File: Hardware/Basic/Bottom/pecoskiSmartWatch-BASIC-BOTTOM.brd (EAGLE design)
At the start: 33 x 33 mm, 31 parts, among them U1 AD5242-SO16

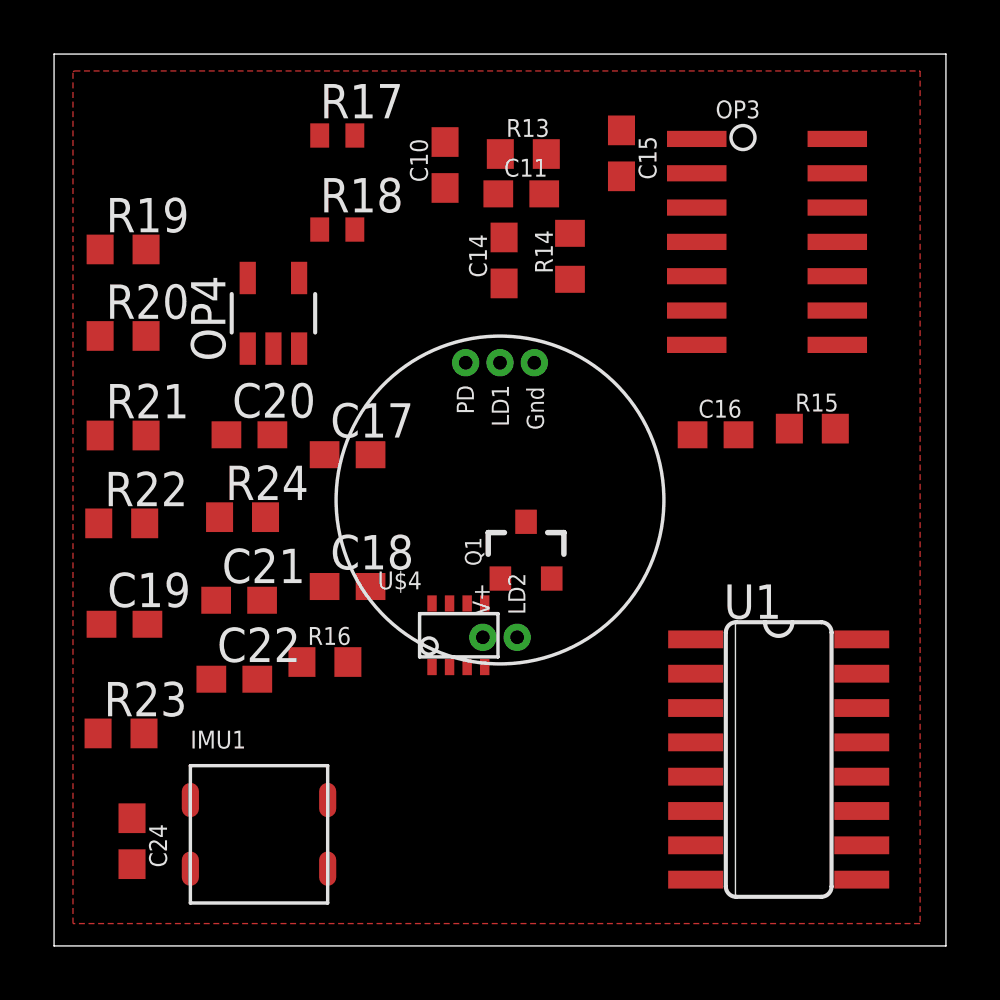
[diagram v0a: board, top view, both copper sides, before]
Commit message: Updated Eagle Hardware 2021_02_27
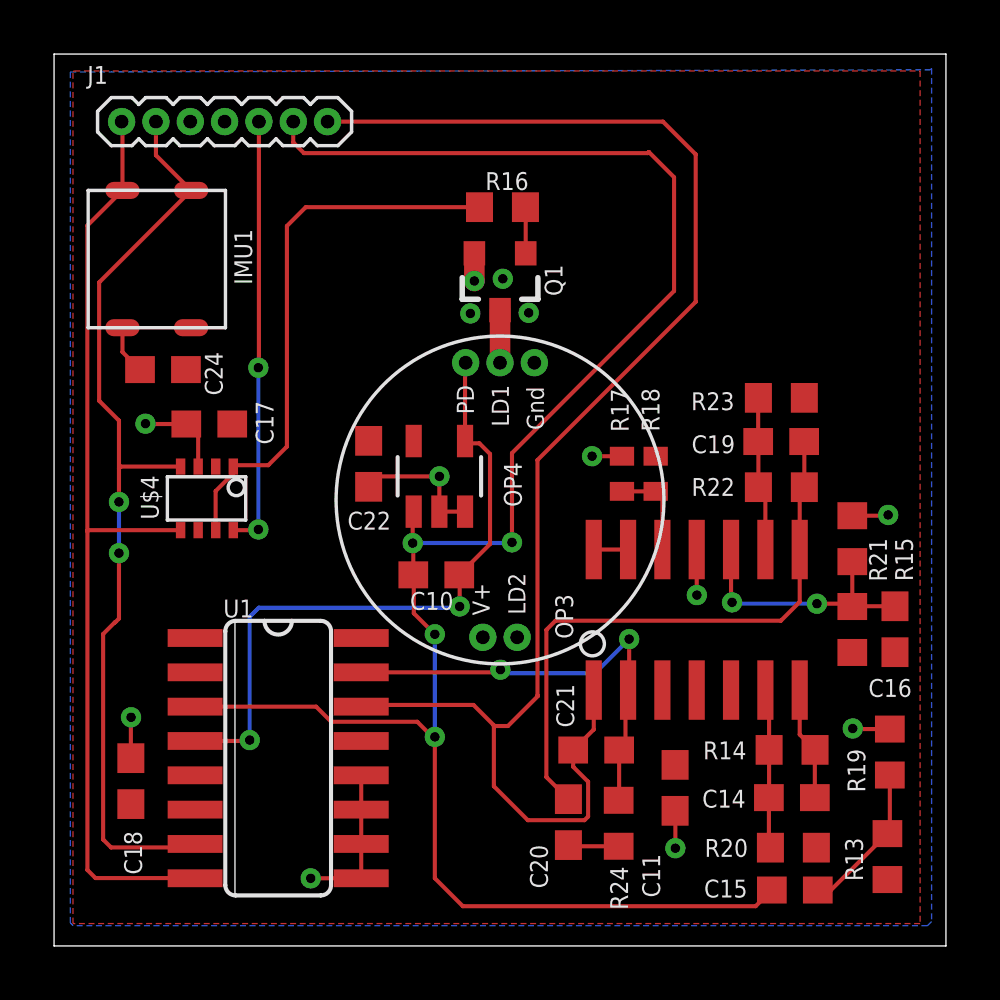
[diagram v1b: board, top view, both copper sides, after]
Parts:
- added J1: (no value), LinnesLab-Connectors:1X07_1.27MM
- moved R19 33.9 mm to (33.4, 9.67), turned to 270 degrees
- moved R20 31.2 mm to (29.9, 6.14), turned to 180 degrees
- moved R13 29.3 mm to (33.3, 5.81), turned to 270 degrees
- moved C15 28.0 mm to (29.9, 4.57), turned to 0 degrees
- moved R23 27.4 mm to (29.4, 22.8), turned to 180 degrees
- moved R21 27.2 mm to (32.0, 17.6), turned to 270 degrees
- moved C19 25.2 mm to (29.4, 21.2), turned to 180 degrees
- moved R22 24.4 mm to (29.4, 19.5)
- moved C11 22.7 mm to (25.5, 8.35), turned to 90 degrees
- moved C14 22.5 mm to (29.8, 7.99), turned to 180 degrees
- moved IMU1 21.6 mm to (6.30, 27.9), turned to 90 degrees
- moved R14 20.0 mm to (29.8, 9.75), turned to 0 degrees
- moved C20 18.6 mm to (21.5, 7.08), turned to 270 degrees
- moved U1 18.5 mm to (10.8, 9.45)
- moved R16 18.1 mm to (19.1, 29.8)
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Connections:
- removed net LED: Q1.3
- removed net LED.CTRL: U$4.8
- removed net PPG: C21.2, OP3.1, U1.14
- removed net TIA: C10.2, C15.1, OP4.1, U1.3
- new net A6/TIA: C10.2, C15.1, J1.6, OP4.1, U1.3
- new net A7/PPG: C21.2, J1.7, OP3.1, U1.14
- new net D29/LED.CTRL: J1.5, U$4.8
- net 3.3V: now also J1.4
- net GND: now also J1.3
- net LED.C: now also Q1.3
- net SCL: now also J1.2
- net SDA: now also J1.1
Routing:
- net A6/TIA: track 0.00 -> 71.5 mm, vias 0 -> 4
- net A7/PPG: track 0.00 -> 55.5 mm
- net SDA: track 0.00 -> 35.8 mm
- net SCL: track 0.00 -> 35.0 mm, vias 0 -> 2
- net GND: track 0.00 -> 25.2 mm, vias 0 -> 13
- net PD.C: track 0.00 -> 24.7 mm, vias 0 -> 2
- net N$19: track 0.00 -> 22.5 mm
- net N$9: track 0.00 -> 20.5 mm
- net G.W2: track 0.00 -> 16.7 mm, vias 0 -> 2
- net D29/LED.CTRL: track 0.00 -> 16.0 mm, vias 0 -> 2
- net N$17: track 0.00 -> 9.73 mm, vias 0 -> 2
- net N$15: track 0.00 -> 5.91 mm
- net N$18: track 0.00 -> 5.73 mm
- net N$13: track 0.00 -> 5.65 mm
- net N$16: track 0.00 -> 4.22 mm
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- added copper zone on layer 16, net GND

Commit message: Hardware Updates 2021_02_27
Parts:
- moved R23 0.53 mm to (29.4, 23.3)
- moved R20 0.48 mm to (29.7, 6.59)
- moved R15 0.45 mm to (31.7, 14.5)
- moved R14 0.42 mm to (29.7, 10.2)
- moved C16 0.38 mm to (33.4, 14.6)
- moved C14 0.36 mm to (29.7, 8.32)
- moved R21 0.34 mm to (32.0, 17.9)
- moved OP3 0.34 mm to (26.2, 14.9)
- moved R13 0.33 mm to (33.4, 5.48)
- moved C19 0.28 mm to (29.4, 21.4)
- moved R22 0.28 mm to (29.4, 19.8)
- moved R17 0.26 mm to (24.7, 20.2)
- moved R18 0.26 mm to (23.5, 20.2)
- moved C21 0.19 mm to (22.6, 9.94)
- renumbered OP4 to TIA, U$4 to AD517, U1 to AD5242
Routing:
- net VREF: track 1.27 -> 34.1 mm, vias 0 -> 3
- net N$13: track 5.65 -> 16.1 mm
- net N$16: track 4.22 -> 8.72 mm
- net GND: track 25.2 -> 26.6 mm, vias 13 -> 14
- net N$17: track 9.73 -> 10.9 mm

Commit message: HW Updates 2021/03/06
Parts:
- added C1: 100n, LinnesLab-Passives:C0603
- added LOGO1: REVISION.A, LinnesLab-Logos:REV.A
- added LOGO2: OSHW-LOGOS, LinnesLab-Logos:OSHW-LOGO-S
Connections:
- net GND: now also C1.2
- net VREF: now also C1.1
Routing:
- net GND: track 26.6 -> 28.2 mm, vias 14 -> 15
- net VREF: track 34.1 -> 35.5 mm
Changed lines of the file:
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@@
 <attribute name="VALUE" x="3.73" y="30.968" locked="yes" size="0.6096" layer="27" font="vector" ratio="20"/>
 </element>
+<element name="C1" library="LinnesLab-Passives" package="C0603" value="100n" x="28.582625" y="26.461721875" smashed="yes" rot="R90">
+<attribute name="NAME" x="27.614884375" y="26.174703125" size="0.7112" layer="25" rot="R90"/>
+<attribute name="VALUE" x="30.487625" y="25.826721875" size="1.27" layer="27" rot="R90"/>
+</element>
+<element name="LOGO1" library="LinnesLab-Logos" package="REV.A" value="REVISION.A" x="4.03098125" y="3.850640625" smashed="yes"/>
+<element name="LOGO2" library="LinnesLab-Logos" package="OSHW-LOGO-S" value="OSHW-LOGOS" x="32.19958125" y="32.362140625" smashed="yes"/>
 </elements>
 <signals>
@@
 <wire x1="5.0317375" y1="26.037534375" x2="5.509259375" y2="26.51505625" width="0.1524" layer="1"/>
 <via x="5.509259375" y="26.51505625" extent="1-16" drill="0.35"/>
+<contactref element="C1" pad="2"/>
+<wire x1="28.582625" y1="27.311721875" x2="28.582625" y2="28.897584375" width="0.1524" layer="1"/>
+<wire x1="28.582625" y1="28.897584375" x2="28.5877" y2="28.902659375" width="0.1524" layer="1"/>
+<via x="28.5877" y="28.902659375" extent="1-16" drill="0.35"/>
 </signal>
 <signal name="3.3V">
@@
 <wire x1="22.438353125" y1="19.959690625" x2="21.7731375" y2="20.62490625" width="0.1524" layer="1"/>
 <wire x1="21.7731375" y1="20.62490625" x2="21.7731375" y2="21.19655625" width="0.1524" layer="1"/>
-<wire x1="21.7731375" y1="21.19655625" x2="25.1968" y2="24.62021875" width="0.1524" layer="1"/>
-<wire x1="30.2759" y1="24.252821875" x2="30.2759" y2="23.340059375" width="0.1524" layer="1"/>
-<wire x1="30.2759" y1="23.340059375" x2="30.242878125" y2="23.3070375" width="0.1524" layer="1"/>
-<wire x1="25.1968" y1="24.62021875" x2="29.908503125" y2="24.62021875" width="0.1524" layer="1"/>
-<wire x1="29.908503125" y1="24.62021875" x2="30.2759" y2="24.252821875" width="0.1524" layer="1"/>
+<wire x1="30.242878125" y1="23.309578125" x2="30.242878125" y2="23.3070375" width="0.1524" layer="1"/>
 <wire x1="30.562915625" y1="6.591296875" x2="31.292796875" y2="6.591296875" width="0.1524" layer="1"/>
 <wire x1="31.292796875" y1="6.591296875" x2="31.709359375" y2="7.007859375" width="0.1524" layer="1"/>
@@
 <wire x1="23.6728" y1="15.621" x2="25.003759375" y2="14.290040625" width="0.1524" layer="16"/>
 <wire x1="25.003759375" y1="14.290040625" x2="25.003759375" y2="14.26998125" width="0.1524" layer="16"/>
+<contactref element="C1" pad="1"/>
+<wire x1="26.188303125" y1="25.611721875" x2="28.582625" y2="25.611721875" width="0.1524" layer="1"/>
+<wire x1="21.7731375" y1="21.19655625" x2="26.188303125" y2="25.611721875" width="0.1524" layer="1"/>
+<wire x1="28.582625" y1="25.611721875" x2="29.793296875" y2="25.611721875" width="0.1524" layer="1"/>
+<wire x1="29.793296875" y1="25.611721875" x2="30.261559375" y2="25.143459375" width="0.1524" layer="1"/>
+<wire x1="30.261559375" y1="25.143459375" x2="30.261559375" y2="23.328259375" width="0.1524" layer="1"/>
+<wire x1="30.261559375" y1="23.328259375" x2="30.242878125" y2="23.309578125" width="0.1524" layer="1"/>
 </signal>
 <signal name="N$9">

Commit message: Updated HW 2021_03_13 AM
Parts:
- added C2: 1u, LinnesLab-Passives:C0603
- added U2: PCF8523, LinnesLab-Clocks:SO8
- added Y2: 32.7680kHz, LinnesLab-Clocks:2-SMD.NOLEAD.2.0MMTO1.2MM
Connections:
- new net N$1: U2.2, Y2.P$1
- new net N$2: U2.1, Y2.P$2
- new net VBAT: U2.3
- net 3.3V: now also C2.1, U2.8
- net GND: now also C2.2, U2.4
- net SCL: now also U2.6
- net SDA: now also U2.5

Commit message: Updated HW 2021_03_13 PM
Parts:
- added C3, C4: 4.7u, LinnesLab-Passives:C0603
- added C6, C9: 1u, LinnesLab-Passives:C0603
- added CHRG: MCP73831, LinnesLab-Power:SOT23-5
- added LDO1: MIC5504, LinnesLab-Power:SOT23-5
- added R3: 100k, LinnesLab-Passives:R0603
- added R4: (no value), LinnesLab-Passives:R0603
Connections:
- new net D27/CHRG.STATUS: CHRG.1, R3.1
- new net N$3: CHRG.5, R4.2
- new net VIN1: C4.2, C6.2, CHRG.4, LDO1.1, LDO1.3, R3.2
- new net VLIPO: C3.1, CHRG.3
- net 3.3V: now also C9.1, LDO1.5
- net GND: now also C3.2, C4.1, C6.1, C9.2, CHRG.2, LDO1.2, R4.1
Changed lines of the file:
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@@
 <attribute name="VALUE" x="-13.675359375" y="-7.566659375" size="0.7112" layer="27"/>
+</element>
+<element name="CHRG" library="LinnesLab-Power" package="SOT23-5" value="MCP73831" x="-12.36218125" y="-14.54658125" smashed="yes">
+<attribute name="NAME" x="-14.26718125" y="-14.54658125" size="0.6096" layer="25" ratio="20" rot="R90" align="bottom-center"/>
+<attribute name="PROD_ID" value="IC-09995" x="-12.36218125" y="-14.157959375" size="1.778" layer="27" display="off"/>
+<attribute name="VALUE" x="-9.82218125" y="-14.54658125" size="0.6096" layer="27" ratio="20" rot="R90" align="bottom-center"/>
+</element>
+<element name="LDO1" library="LinnesLab-Power" package="SOT23-5" value="MIC5504" x="-9.357359375" y="-23.014940625" smashed="yes">
+<attribute name="NAME" x="-11.262359375" y="-23.014940625" size="0.6096" layer="25" ratio="20" rot="R90" align="bottom-center"/>
+<attribute name="VALUE" x="-6.817359375" y="-23.014940625" size="0.6096" layer="27" ratio="20" rot="R90" align="bottom-center"/>
+</element>
+<element name="C6" library="LinnesLab-Passives" package="C0603" package3d_urn="urn:adsk.eagle:package:15661989/2" value="1u" x="-7.49808125" y="-18.59788125" smashed="yes">
+<attribute name="NAME" x="-8.13308125" y="-17.96288125" size="0.7112" layer="25"/>
+<attribute name="VALUE" x="-8.13308125" y="-20.50288125" size="0.7112" layer="27"/>
+</element>
+<element name="C9" library="LinnesLab-Passives" package="C0603" package3d_urn="urn:adsk.eagle:package:15661989/2" value="1u" x="-13.67028125" y="-22.672040625" smashed="yes">
+<attribute name="NAME" x="-14.30528125" y="-22.037040625" size="0.7112" layer="25"/>
+<attribute name="VALUE" x="-14.30528125" y="-24.577040625" size="0.7112" layer="27"/>
+</element>
+<element name="C3" library="LinnesLab-Passives" package="C0603" package3d_urn="urn:adsk.eagle:package:15661989/2" value="4.7u" x="-13.67028125" y="-18.59788125" smashed="yes">
+<attribute name="NAME" x="-14.30528125" y="-17.96288125" size="0.7112" layer="25"/>
+<attribute name="VALUE" x="-14.30528125" y="-20.50288125" size="0.7112" layer="27"/>
+</element>
+<element name="C4" library="LinnesLab-Passives" package="C0603" package3d_urn="urn:adsk.eagle:package:15661989/2" value="4.7u" x="-10.58418125" y="-18.59788125" smashed="yes">
+<attribute name="NAME" x="-11.21918125" y="-17.96288125" size="0.7112" layer="25"/>
+<attribute name="VALUE" x="-11.21918125" y="-20.50288125" size="0.7112" layer="27"/>
+</element>
+<element name="R4" library="LinnesLab-Passives" package="R0603" package3d_urn="urn:adsk.eagle:package:15661944/2" value="" x="-13.67281875" y="-26.7462" smashed="yes">
+<attribute name="NAME" x="-14.30781875" y="-26.1112" size="0.7112" layer="25"/>
+<attribute name="VALUE" x="-14.30781875" y="-28.6512" size="0.7112" layer="27"/>
+</element>
+<element name="R3" library="LinnesLab-Passives" package="R0603" package3d_urn="urn:adsk.eagle:package:15661944/2" value="100k" x="-7.81558125" y="-13.815059375" smashed="yes">
+<attribute name="NAME" x="-8.45058125" y="-13.180059375" size="0.7112" layer="25"/>
+<attribute name="VALUE" x="-8.45058125" y="-15.720059375" size="0.7112" layer="27"/>
 </element>
 </elements>
@@
 <contactref element="U2" pad="4"/>
 <contactref element="C2" pad="2"/>
+<contactref element="C6" pad="1"/>
+<contactref element="LDO1" pad="2"/>
+<contactref element="C9" pad="2"/>
+<contactref element="C3" pad="2"/>
+<contactref element="R4" pad="1"/>
+<contactref element="C4" pad="1"/>
+<contactref element="CHRG" pad="2"/>
 <wire x1="23.4848375" y1="20.876021875" x2="28.582625" y2="27.311721875" width="0" layer="19" extent="1-1"/>
 <wire x1="20.27" y1="24.08" x2="22.3799375" y2="20.87625625" width="0" layer="19" extent="1-1"/>
@@
 <wire x1="11.99641875" y1="5.001259375" x2="5.341625" y2="9.447903125" width="0" layer="19" extent="1-1"/>
 <wire x1="-6.543940625" y1="-9.73581875" x2="5.341625" y2="9.447903125" width="0" layer="19" extent="1-1"/>
+<wire x1="-12.36218125" y1="-15.84668125" x2="-6.543940625" y2="-9.73581875" width="0" layer="19" extent="1-1"/>
+<wire x1="-12.82028125" y1="-18.59788125" x2="-12.36218125" y2="-15.84668125" width="0" layer="19" extent="1-1"/>
+<wire x1="-11.43418125" y1="-18.59788125" x2="-12.82028125" y2="-18.59788125" width="0" layer="19" extent="1-1"/>
+<wire x1="-8.34808125" y1="-18.59788125" x2="-11.43418125" y2="-18.59788125" width="0" layer="19" extent="1-1"/>
+<wire x1="-12.82028125" y1="-22.672040625" x2="-12.82028125" y2="-18.59788125" width="0" layer="19" extent="1-1"/>
+<wire x1="-9.357359375" y1="-24.315040625" x2="-12.82028125" y2="-22.672040625" width="0" layer="19" extent="1-1"/>
+<wire x1="-14.52281875" y1="-26.7462" x2="-12.82028125" y2="-22.672040625" width="0" layer="19" extent="1-1"/>
 <wire x1="-14.420359375" y1="-5.915659375" x2="-6.543940625" y2="-9.73581875" width="0" layer="19" extent="1-1"/>
 </signal>
@@
 <contactref element="U2" pad="8"/>
 <contactref element="C2" pad="1"/>
+<contactref element="LDO1" pad="5"/>
+<contactref element="C9" pad="1"/>
 <wire x1="26.248353125" y1="12.3098" x2="24.731978125" y2="20.8760125" width="0" layer="19" extent="1-1"/>
 <wire x1="25.47873125" y1="9.1989875" x2="26.248353125" y2="12.3098" width="0" layer="19" extent="1-1"/>
@@
 <wire x1="-9.120359375" y1="-2.105659375" x2="5.341625" y2="7.747903125" width="0" layer="19" extent="1-1"/>
 <wire x1="-8.243940625" y1="-9.73581875" x2="-9.120359375" y2="-2.105659375" width="0" layer="19" extent="1-1"/>
+<wire x1="-10.307359375" y1="-21.714840625" x2="-8.243940625" y2="-9.73581875" width="0" layer="19" extent="1-1"/>
+<wire x1="-14.52028125" y1="-22.672040625" x2="-10.307359375" y2="-21.714840625" width="0" layer="19" extent="1-1"/>
 </signal>
 <signal name="SDA">
@@
 <wire x1="-14.420359375" y1="-2.105659375" x2="-12.029540625" y2="-9.95171875" width="0" layer="19" extent="1-1"/>
 </signal>
+<signal name="N$3">
+<contactref element="CHRG" pad="5"/>
+<contactref element="R4" pad="2"/>
+<wire x1="-13.31218125" y1="-13.24648125" x2="-12.82281875" y2="-26.7462" width="0" layer="19" extent="1-1"/>
+</signal>
+<signal name="VLIPO">
+<contactref element="CHRG" pad="3"/>
+<contactref element="C3" pad="1"/>
+<wire x1="-11.41218125" y1="-15.84668125" x2="-14.52028125" y2="-18.59788125" width="0" layer="19" extent="1-1"/>
+</signal>
+<signal name="VIN1">
+<contactref element="C6" pad="2"/>
+<contactref element="LDO1" pad="1"/>
+<contactref element="LDO1" pad="3"/>
+<contactref element="CHRG" pad="4"/>
+<contactref element="C4" pad="2"/>
+<contactref element="R3" pad="2"/>
+<wire x1="-8.407359375" y1="-24.315040625" x2="-10.307359375" y2="-24.315040625" width="0" layer="19" extent="1-1"/>
+<wire x1="-9.73418125" y1="-18.59788125" x2="-10.307359375" y2="-24.315040625" width="0" layer="19" extent="1-1"/>
+<wire x1="-6.64808125" y1="-18.59788125" x2="-9.73418125" y2="-18.59788125" width="0" layer="19" extent="1-1"/>
+<wire x1="-6.96558125" y1="-13.815059375" x2="-6.64808125" y2="-18.59788125" width="0" layer="19" extent="1-1"/>
+<wire x1="-11.41218125" y1="-13.24648125" x2="-6.96558125" y2="-13.815059375" width="0" layer="19" extent="1-1"/>
+</signal>
+<signal name="D27/CHRG.STATUS">
+<contactref element="R3" pad="1"/>
+<contactref element="CHRG" pad="1"/>
+<wire x1="-8.66558125" y1="-13.815059375" x2="-13.31218125" y2="-15.84668125" width="0" layer="19" extent="1-1"/>
+</signal>
 </signals>
